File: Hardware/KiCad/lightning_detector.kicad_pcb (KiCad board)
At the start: 2 copper layers, 73.7 x 78.7 mm, 51 parts, among them J1 PinHeader_1x07_P2.54mm_Horizo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, J2 PinHeader_1x02_P2.54mm_Horizo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, J3 SolderWirePad_1x01_SMD_1x2mm, J4 SolderWirePad_1x01_SMD_1x2mm, J5 SolderWirePad_1x01_SMD_1x2mm, J6 SolderWirePad_1x01_SMD_1x2mm, J7 PinHeader_1x02_P2.54mm_Horizo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, Q1 TO-92, SW1 PinHeader_1x03_P2.54mm_Vertic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, SW2 SW_DIP_SPSTx08_Slide_9.78x22.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

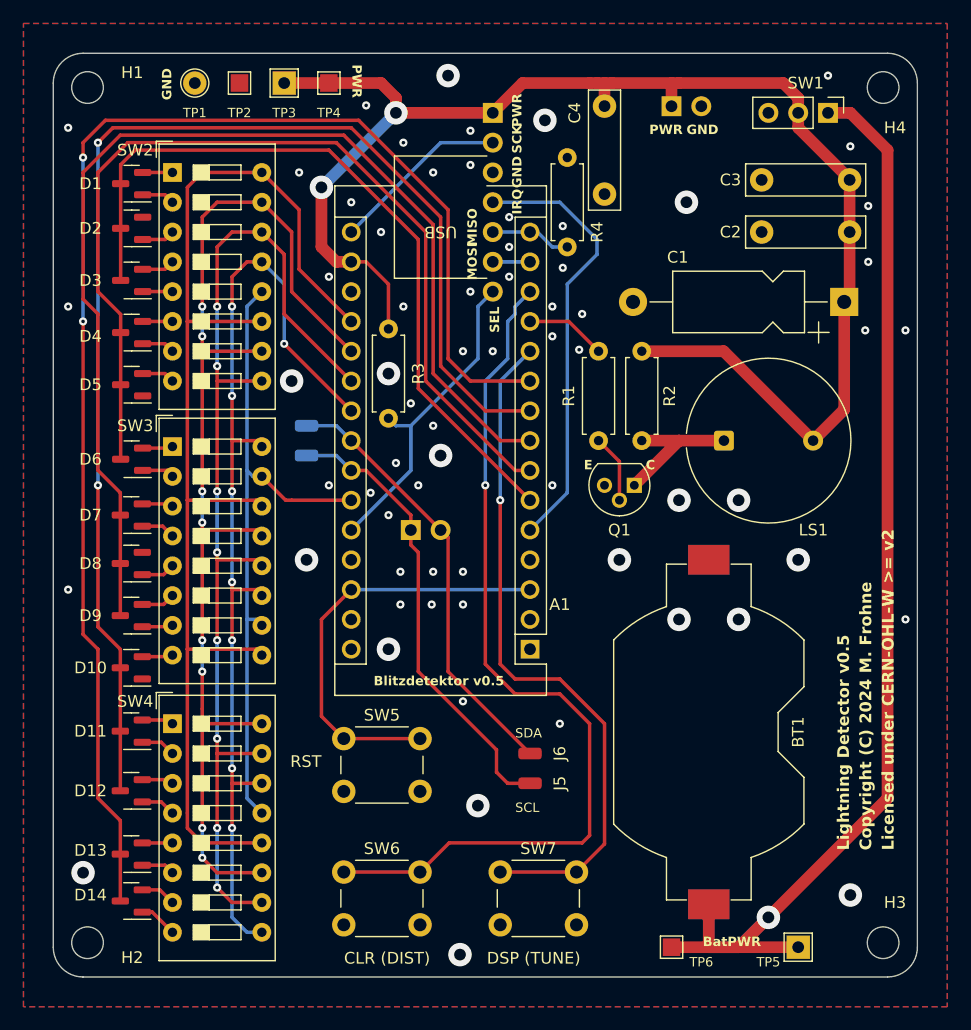
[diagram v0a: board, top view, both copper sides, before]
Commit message: Update design files to KiCad version 8 and fix footprint overlap.
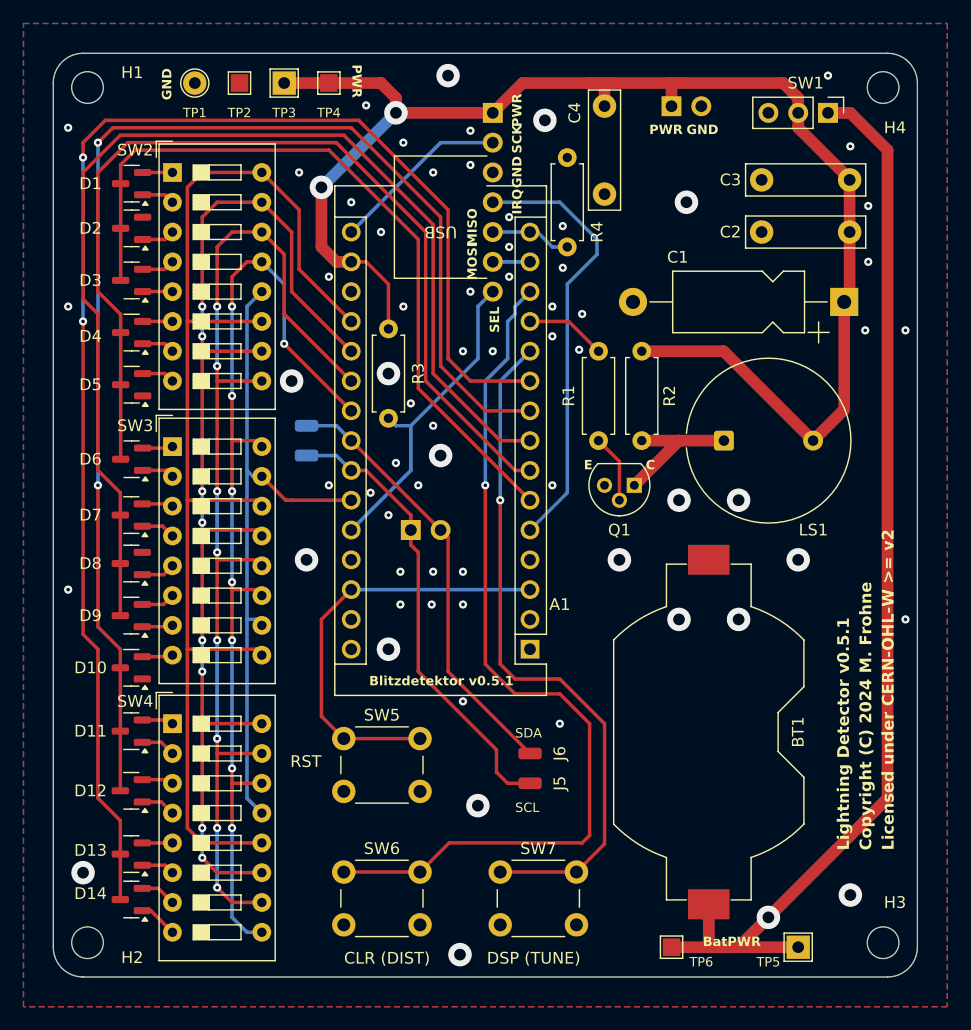
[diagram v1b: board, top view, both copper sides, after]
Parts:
- moved D14 0.13 mm to (34.6, 89.9)
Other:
- board text added: "Blitzdetektor v0.5.1"
- board text added: "Lightning Detector v0.5.1"
- board text added: "Lightning Detector v0.5.1 Copyright (C) 2024 M. Frohne Licensed under CERN-OHL-W version 2, or (at your option) any later version"
- board text removed: "Blitzdetektor v0.5"
- board text removed: "Lightning Detector v0.5"
- board text removed: "Lightning Detector v0.5 Copyright (C) 2024 M. Frohne Licensed under CERN-OHL-W version 2, or (at your option) any later version"

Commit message: Update copyright years.
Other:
- board text added: "Copyright (C) 2024-2025 M. Frohne"
- board text added: "Lightning Detector v0.5.1 Copyright (C) 2024-2025 M. Frohne Licensed under CERN-OHL-W version 2, or (at your option) any later version"
- board text removed: "Copyright (C) 2024 M. Frohne"
- board text removed: "Lightning Detector v0.5.1 Copyright (C) 2024 M. Frohne Licensed under CERN-OHL-W version 2, or (at your option) any later version"
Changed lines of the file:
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@@
 		)
 	)
-	(gr_text "Copyright (C) 2024 M. Frohne"
+	(gr_text "Copyright (C) 2024-2025 M. Frohne"
 		(at 97.79 85.725 90)
 		(layer "F.SilkS")
@@
 		)
 	)
-	(gr_text "Lightning Detector v0.5.1\nCopyright (C) 2024 M. Frohne\nLicensed under CERN-OHL-W version 2, or (at your option) any later version"
+	(gr_text "Lightning Detector v0.5.1\nCopyright (C) 2024-2025 M. Frohne\nLicensed under CERN-OHL-W version 2, or (at your option) any later version"
 		(at 35.56 106.68 0)
 		(layer "Cmts.User")
@@
 		)
 	)
-	(gr_text "Lightning Detector v0.5.1\nCopyright (C) 2024 M. Frohne\nLicensed under CERN-OHL-W version 2, or (at your option) any later version"
+	(gr_text "Lightning Detector v0.5.1\nCopyright (C) 2024-2025 M. Frohne\nLicensed under CERN-OHL-W version 2, or (at your option) any later version"
 		(at 35.56 106.68 0)
 		(layer "F.Fab")
